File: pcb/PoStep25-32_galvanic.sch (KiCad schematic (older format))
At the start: 10 parts, among them P3 PoStep25-32, Q11 BSS138, U9 LTV-847

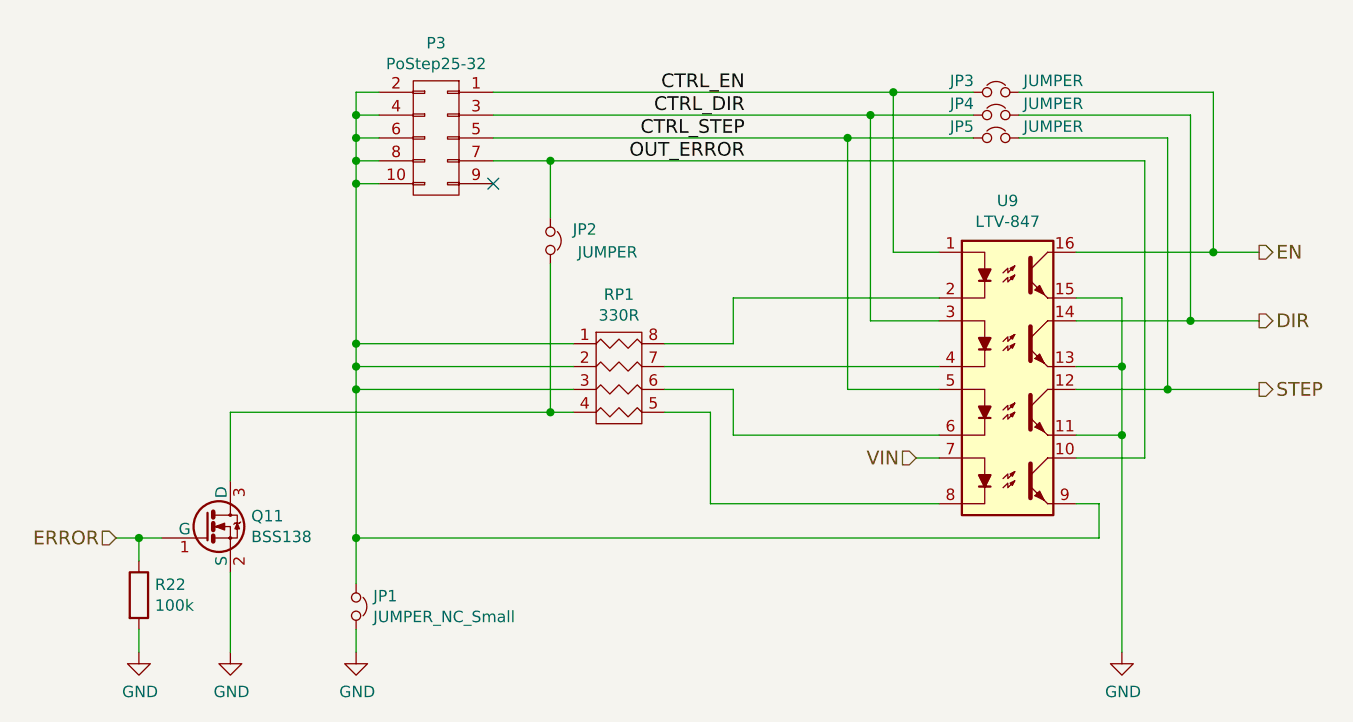
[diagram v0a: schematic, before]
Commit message: Place remaining components onto pcb, remove galvanic protection circuit
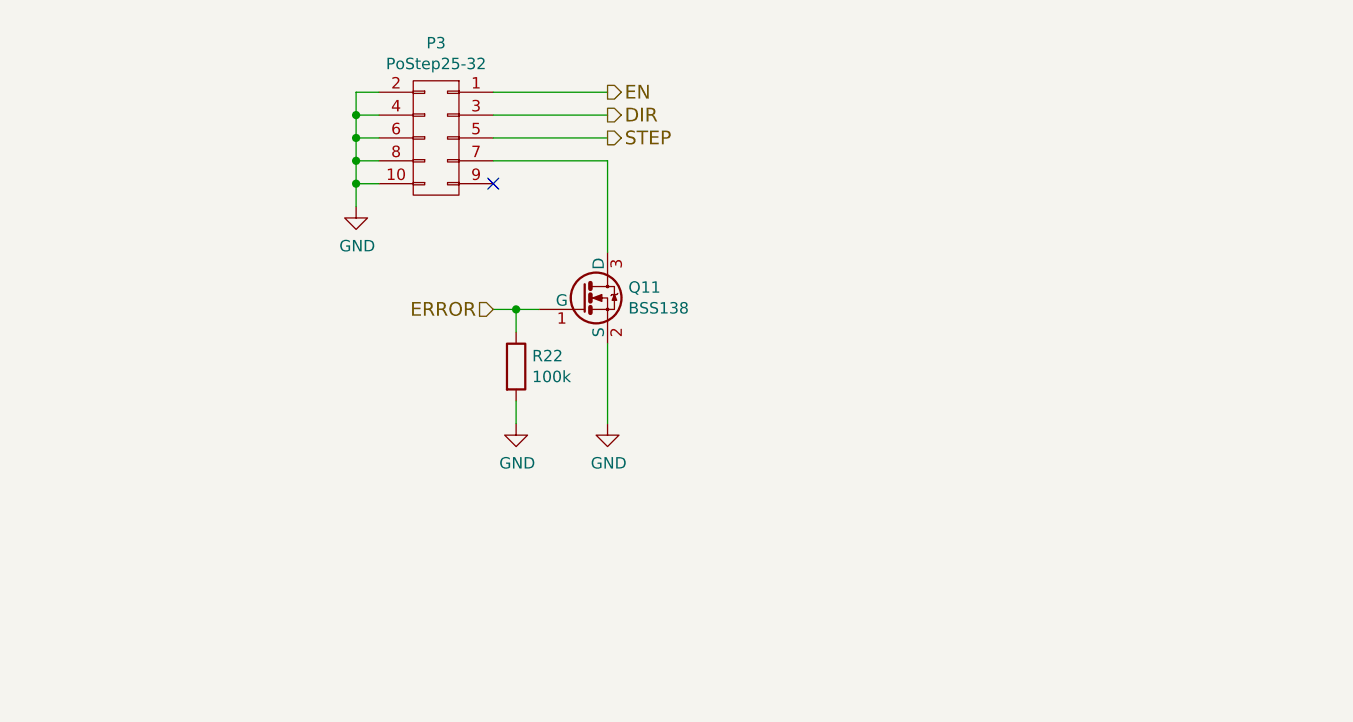
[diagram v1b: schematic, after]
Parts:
- removed JP1: JUMPER_NC_Small, Jumpers_SMD:JUMPER-SOLDER-SMD, symbol JUMPER_NC_Small
- removed JP2, JP3, JP4, JP5: JUMPER, Jumpers_SMD:JUMPER-SOLDER-SMD, symbol JUMPER_NC_Small
- removed RP1: 330R, Resistors_SMD:R_Array_Convex_4x0603, symbol R_PACK4
- removed U9: LTV-847, Opto-Devices:Optocoupler_SMD_LTV-847S, symbol LTV-847
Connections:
- net CTRL_DIR is gone; now on net DIR: P3.3 (P3)
- net CTRL_EN is gone; now on net EN: P3.1 (P1)
- net CTRL_STEP is gone; now on net STEP: P3.5 (P5)
- net OUT_ERROR is gone; now on an unnamed net: P3.7 (P7)
- net GND: now also P3.10 (P10), P3.2 (P2), P3.4 (P4), P3.6 (P6), P3.8 (P8)
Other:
- moved on the sheet: Q11, R22

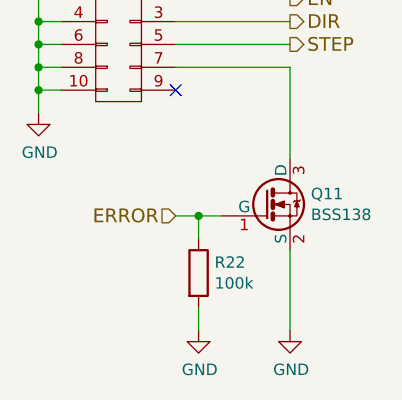
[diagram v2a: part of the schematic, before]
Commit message: Add some little changes to the schematic, add calculations
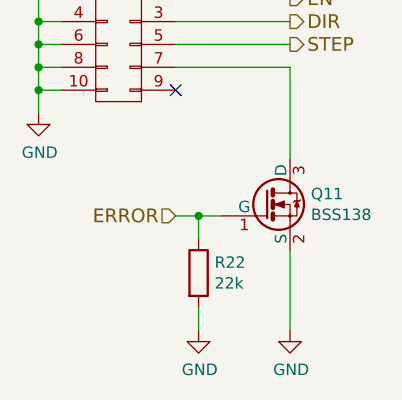
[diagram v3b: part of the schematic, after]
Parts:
- R22: value 100k -> 22k
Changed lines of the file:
@@
 NoConn ~ 4900 3050
 $Comp
-L GND #PWR089
+L GND #PWR090
 U 1 1 581072C7
 P 4300 3150
-F 0 "#PWR089" H 4300 2900 50  0001 C CNN
+F 0 "#PWR090" H 4300 2900 50  0001 C CNN
 F 1 "GND" H 4305 2977 50  0000 C CNN
 F 2 "" H 4300 3150 50  0000 C CNN
@@
 P 5000 3850
 F 0 "R22" H 5070 3896 50  0000 L CNN
-F 1 "100k" H 5070 3805 50  0000 L CNN
+F 1 "22k" H 5070 3805 50  0000 L CNN
 F 2 "Resistors_SMD:R_0603" V 4930 3850 50  0001 C CNN
 F 3 "" H 5000 3850 50  0000 C CNN
@@
 $EndComp
 $Comp
-L GND #PWR090
+L GND #PWR091
 U 1 1 58115D99
 P 5400 4100
-F 0 "#PWR090" H 5400 3850 50  0001 C CNN
+F 0 "#PWR091" H 5400 3850 50  0001 C CNN
 F 1 "GND" H 5405 3927 50  0000 C CNN
 F 2 "" H 5400 4100 50  0000 C CNN
@@
 $EndComp
 $Comp
-L GND #PWR091
+L GND #PWR092
 U 1 1 58115DC2
 P 5000 4100
-F 0 "#PWR091" H 5000 3850 50  0001 C CNN
+F 0 "#PWR092" H 5000 3850 50  0001 C CNN
 F 1 "GND" H 5005 3927 50  0000 C CNN
 F 2 "" H 5000 4100 50  0000 C CNN

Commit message: Add more order informations, create BOM
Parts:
- Q11: Digi-Key Minimum Quantity (none) -> 1; Digi-Key Part Number (none) -> BSS138NH6327XTSA2CT-ND
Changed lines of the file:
@@
 F 1 "BSS138" H 5491 3505 50  0000 L CNN
 F 2 "TO_SOT_Packages_SMD:SOT-23" H 5500 3475 50  0001 L CIN
-F 3 "" H 5300 3550 50  0000 L CNN
+F 3 "http://www.infineon.com/dgdl/Infineon-BSS138N-DS-v02_86-en.pdf?fileId=db3a304330f68606013104d944d53efb" H 5300 3550 50  0001 L CNN
+F 4 "BSS138NH6327XTSA2CT-ND" H 5300 3550 60  0001 C CNN "Digi-Key Part Number"
+F 5 "1" H 5300 3550 60  0001 C CNN "Digi-Key Minimum Quantity"
 	1    5300 3550
 	1    0    0    -1

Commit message: Add more BOM informations
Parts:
- R22: Digi-Key Minimum Quantity (none) -> 5000; Digi-Key Part Number (none) -> 311-22.0KHRTR-ND
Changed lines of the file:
@@
 F 2 "Resistors_SMD:R_0603" V 4930 3850 50  0001 C CNN
 F 3 "" H 5000 3850 50  0000 C CNN
+F 4 "311-22.0KHRTR-ND" H 5000 3850 60  0001 C CNN "Digi-Key Part Number"
+F 5 "5000" H 5000 3850 60  0001 C CNN "Digi-Key Minimum Quantity"
 	1    5000 3850
 	1    0    0    -1

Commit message: Improve BOM
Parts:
- R22: Digi-Key Minimum Quantity 5000 -> 1; Digi-Key Part Number 311-22.0KHRTR-ND -> 311-22.0KHRCT-ND
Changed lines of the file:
@@
 F 2 "Resistors_SMD:R_0603" V 4930 3850 50  0001 C CNN
 F 3 "" H 5000 3850 50  0000 C CNN
-F 4 "311-22.0KHRTR-ND" H 5000 3850 60  0001 C CNN "Digi-Key Part Number"
-F 5 "5000" H 5000 3850 60  0001 C CNN "Digi-Key Minimum Quantity"
+F 4 "311-22.0KHRCT-ND" H 5000 3850 60  0001 C CNN "Digi-Key Part Number"
+F 5 "1" H 5000 3850 60  0001 C CNN "Digi-Key Minimum Quantity"
 	1    5000 3850
 	1    0    0    -1

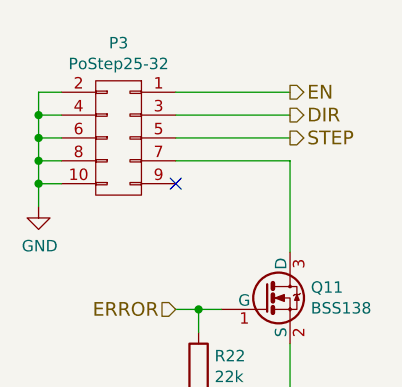
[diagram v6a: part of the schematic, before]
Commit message: Improve layout and add voltage sensing circuit to layout
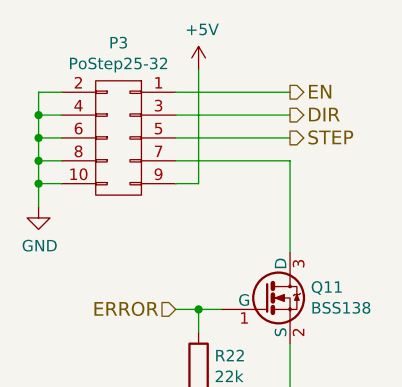
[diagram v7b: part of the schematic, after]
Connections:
- net +5V: now reaches P3.9 (P9)
- no-connect marks 1 -> 0
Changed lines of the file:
@@
 Wire Wire Line
 	4400 2650 4300 2650
-NoConn ~ 4900 3050
 $Comp
-L GND #PWR090
+L GND #PWR095
 U 1 1 581072C7
 P 4300 3150
-F 0 "#PWR090" H 4300 2900 50  0001 C CNN
+F 0 "#PWR095" H 4300 2900 50  0001 C CNN
 F 1 "GND" H 4305 2977 50  0000 C CNN
 F 2 "" H 4300 3150 50  0000 C CNN
@@
 $EndComp
 $Comp
-L GND #PWR091
+L GND #PWR096
 U 1 1 58115D99
 P 5400 4100
-F 0 "#PWR091" H 5400 3850 50  0001 C CNN
+F 0 "#PWR096" H 5400 3850 50  0001 C CNN
 F 1 "GND" H 5405 3927 50  0000 C CNN
 F 2 "" H 5400 4100 50  0000 C CNN
@@
 $EndComp
 $Comp
-L GND #PWR092
+L GND #PWR097
 U 1 1 58115DC2
 P 5000 4100
-F 0 "#PWR092" H 5000 3850 50  0001 C CNN
+F 0 "#PWR097" H 5000 3850 50  0001 C CNN
 F 1 "GND" H 5005 3927 50  0000 C CNN
 F 2 "" H 5000 4100 50  0000 C CNN
@@
 Wire Wire Line
 	4900 2950 5400 2950
+Wire Wire Line
+	4900 3050 5000 3050
+Wire Wire Line
+	5000 3050 5000 2550
+$Comp
+L +5V #PWR098
+U 1 1 583146EE
+P 5000 2550
+F 0 "#PWR098" H 5000 2400 50  0001 C CNN
+F 1 "+5V" H 5015 2723 50  0000 C CNN
+F 2 "" H 5000 2550 50  0000 C CNN
+F 3 "" H 5000 2550 50  0000 C CNN
+	1    5000 2550
+	1    0    0    -1
+$EndComp
 $EndSCHEMATC

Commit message: Add some improvements, fix issue with schematic error
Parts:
- P3: Digi-Key Minimum Quantity (none) -> 1; Digi-Key Part Number (none) -> ED1543-ND
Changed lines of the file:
@@
 LIBS:a4955glptr-t
 LIBS:ap2112k-3.3trg1
+LIBS:lm75bd
+LIBS:mechanical
 LIBS:HighPower-Mechaduino-cache
 EELAYER 25 0
@@
 F 2 "Connectors_Multicomp:Multicomp_MC9A12-1034_2x05x2.54mm_Straight" H 4650 1650 50  0001 C CNN
 F 3 "" H 4650 1650 50  0000 C CNN
+F 4 "ED1543-ND" H 4650 2850 60  0001 C CNN "Digi-Key Part Number"
+F 5 "1" H 4650 2850 60  0001 C CNN "Digi-Key Minimum Quantity"
 	1    4650 2850
 	-1   0    0    -1
@@
 	4400 2650 4300 2650
 $Comp
-L GND #PWR095
+L GND #PWR099
 U 1 1 581072C7
 P 4300 3150
-F 0 "#PWR095" H 4300 2900 50  0001 C CNN
+F 0 "#PWR099" H 4300 2900 50  0001 C CNN
 F 1 "GND" H 4305 2977 50  0000 C CNN
 F 2 "" H 4300 3150 50  0000 C CNN
@@
 $EndComp
 $Comp
-L GND #PWR096
+L GND #PWR0100
 U 1 1 58115D99
 P 5400 4100
-F 0 "#PWR096" H 5400 3850 50  0001 C CNN
+F 0 "#PWR0100" H 5400 3850 50  0001 C CNN
 F 1 "GND" H 5405 3927 50  0000 C CNN
 F 2 "" H 5400 4100 50  0000 C CNN
@@
 $EndComp
 $Comp
-L GND #PWR097
+L GND #PWR0101
 U 1 1 58115DC2
 P 5000 4100
-F 0 "#PWR097" H 5000 3850 50  0001 C CNN
+F 0 "#PWR0101" H 5000 3850 50  0001 C CNN
 F 1 "GND" H 5005 3927 50  0000 C CNN
 F 2 "" H 5000 4100 50  0000 C CNN
@@
 	5000 3050 5000 2550
 $Comp
-L +5V #PWR098
+L +5V #PWR0102
 U 1 1 583146EE
 P 5000 2550
-F 0 "#PWR098" H 5000 2400 50  0001 C CNN
+F 0 "#PWR0102" H 5000 2400 50  0001 C CNN
 F 1 "+5V" H 5015 2723 50  0000 C CNN
 F 2 "" H 5000 2550 50  0000 C CNN
